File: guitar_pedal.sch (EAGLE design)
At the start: 14 parts, among them P1 RM-065

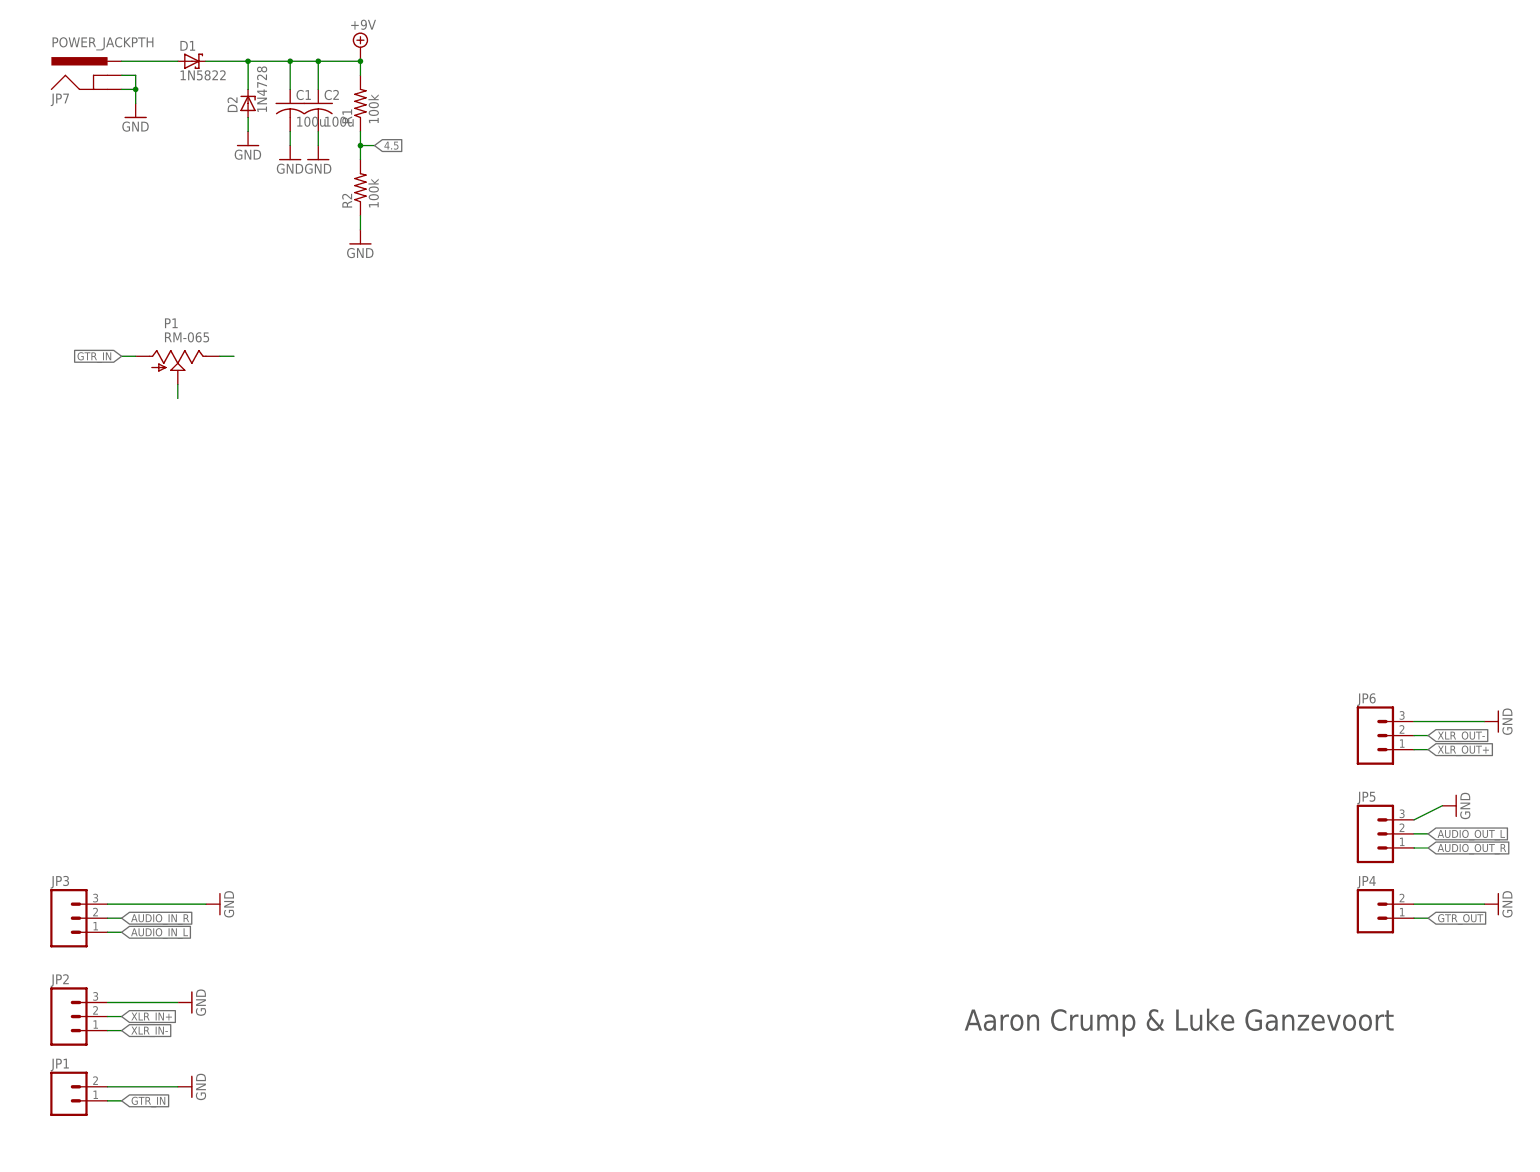
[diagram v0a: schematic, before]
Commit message: mostly finished schematic, still needs stomp switch
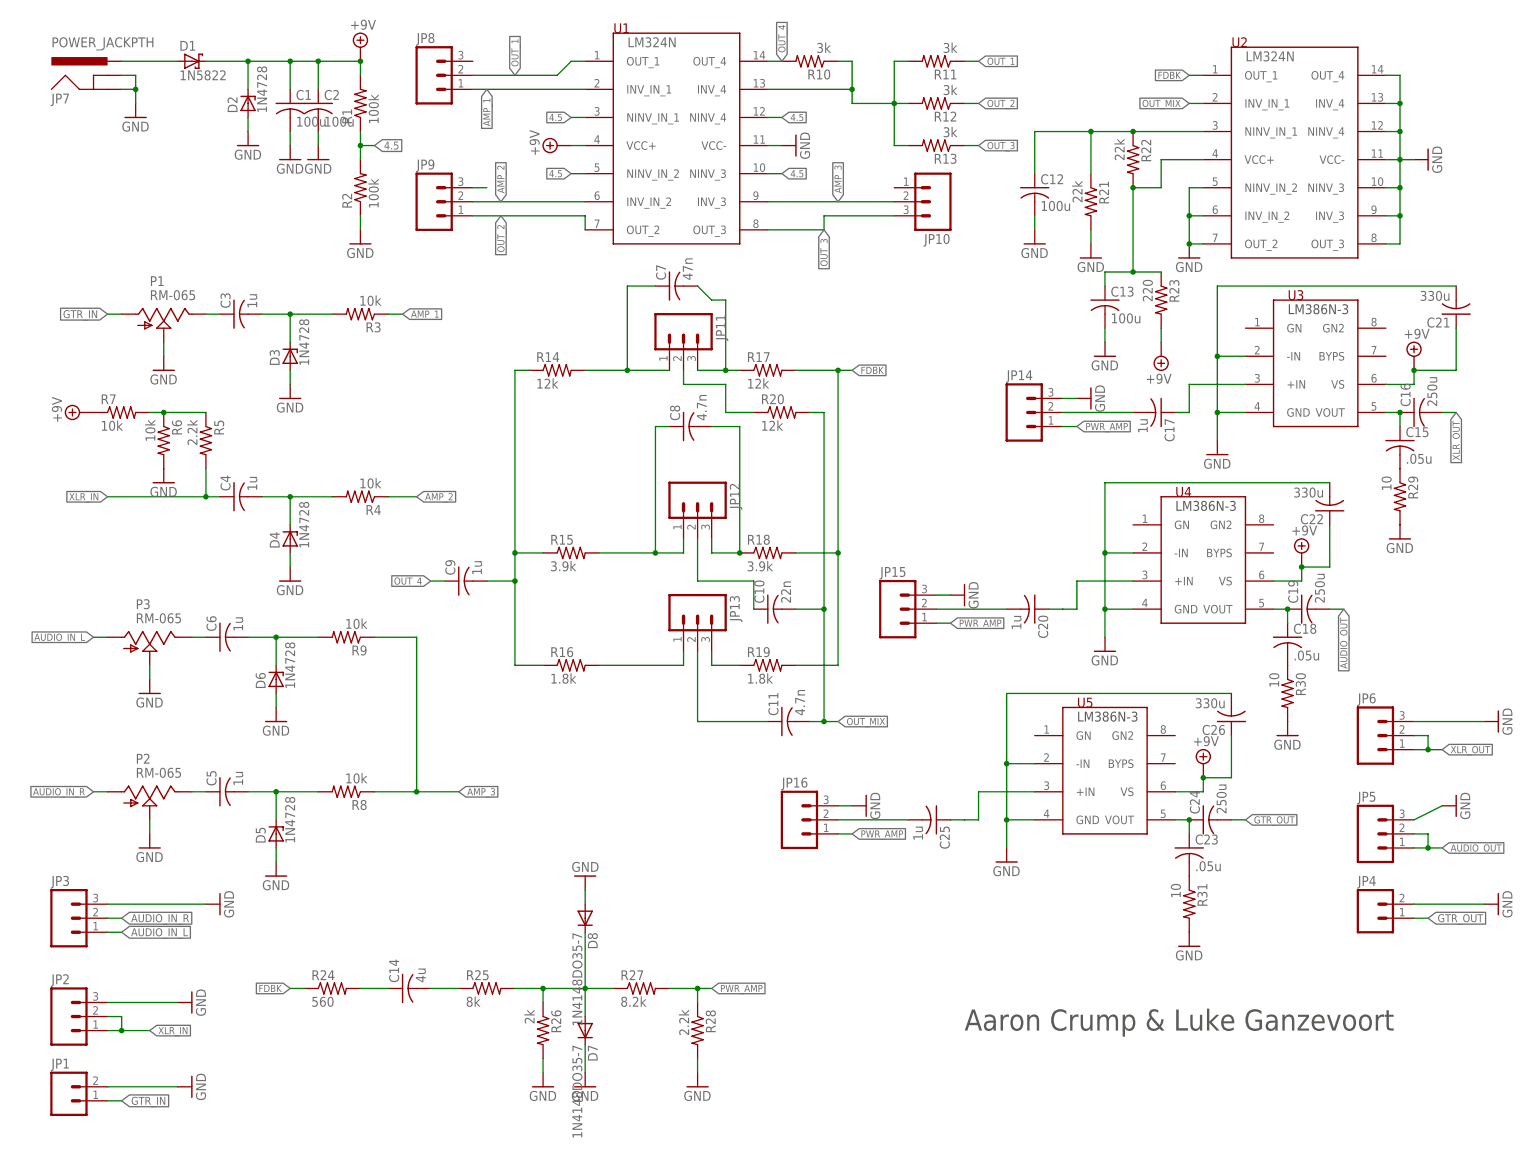
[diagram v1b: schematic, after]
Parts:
- added C10: 22n, resistor:C-USC0805
- added C11, C8: 4.7n, resistor:C-USC0805
- added C12, C13: 100u, resistor:C-USC0805
- added C14: 4u, resistor:C-USC0805
- added C15, C18, C23: .05u, resistor:C-USC0805
- added C16, C19, C24: 250u, resistor:C-USC0805
- added C17, C20, C25, C3, C4, C5, C6, C9: 1u, resistor:C-USC0805
- added C21, C22, C26: 330u, resistor:C-USC0805
- added C7: 47n, resistor:C-USC0805
- added D3, D4, D5, D6: 1N4728, aarons:1N4728
- added D7, D8: 1N4148DO35-7, diode:1N4148DO35-7
- added JP10, JP11, JP12, JP13, JP14, JP15, JP16, JP8, JP9: (no value), SparkFun-Connectors:M03PTH
- added P2, P3: RM-065, aarons:RM-065
- added R10, R11, R12, R13: 3k, resistor:R-US_R0805
- added R14, R17, R20: 12k, resistor:R-US_R0805
- added R15, R18: 3.9k, resistor:R-US_R0805
- added R16, R19: 1.8k, resistor:R-US_R0805
- added R21, R22: 22k, resistor:R-US_R0805
- added R23: 220, resistor:R-US_R0805
- added R24: 560, resistor:R-US_R0805
- added R25: 8k, resistor:R-US_R0805
- added R26: 2k, resistor:R-US_R0805
- added R27: 8.2k, resistor:R-US_R0805
- added R28, R5: 2.2k, resistor:R-US_R0805
- added R29, R30, R31: 10, resistor:R-US_R0805
- added R3, R4, R6, R7, R8, R9: 10k, resistor:R-US_R0805
- added U1, U2: LM324N, aarons:LM324N
- added U3, U4, U5: LM386N-3, aarons:LM386N-3
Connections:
- removed net AUDIO_OUT_L: JP5.2
- removed net AUDIO_OUT_R: JP5.1
- removed net XLR_IN+: JP2.2
- removed net XLR_IN-: JP2.1
- removed net XLR_OUT+: JP6.1
- removed net XLR_OUT-: JP6.2
- new net AMP_1: C3.2, C4.2, C5.2, C6.2, D3.C, D4.C, D5.C, D6.C, JP8.1, R3.1, R3.2, R4.2, R8.2, R9.2, U1.INV_IN_1
- new net AMP_2: JP9.2, JP9.3, R4.1, U1.INV_IN_2
- new net AMP_3: JP10.2, R8.1, R9.1, U1.INV_3
- new net AUDIO_OUT: C19.2, JP5.1, JP5.2
- new net FDBK: R17.2, R18.2, R19.2, R24.1, U2.OUT_1
- new net N$10: C8.1, JP12.1, R15.2
- new net N$11: JP13.1, R16.2
- new net N$12: C9.2, R14.1, R15.1, R16.1
- new net N$13: C11.1, JP13.2
- new net N$14: C14.1, R24.2
- new net N$15: C7.2, JP11.3, R17.1
- new net N$16: C8.2, JP12.3, R18.1
- new net N$17: JP13.3, R19.1
- new net N$18: JP11.2, R20.1
- new net N$19: C10.1, JP12.2
- new net N$20: C14.2, R25.1
- new net N$21: D7.A, D8.C, R25.2, R26.1, R27.1
- new net N$22: C15.2, R29.1
- new net N$23: C17.2, JP14.2
- new net N$24: C13.1, R22.2, R23.1, U2.VCC+
- new net N$25: C18.1, C19.1, U4.VOUT
- new net N$26: C12.1, R21.1, R22.1, U2.NINV_IN_1
- new net N$27: U4.+IN
- new net N$28: C17.1, U3.+IN
- new net N$29: C18.2, R30.1
- new net N$3: R5.1, R6.1, R7.2
- new net N$30: C20.1
- new net N$31: C20.2, JP15.2
- new net N$34: C23.1, C24.1, U5.VOUT
- new net N$35: U5.+IN
- new net N$36: C23.2, R31.1
- new net N$37: C25.1
- new net N$38: C25.2, JP16.2
- new net N$5: C5.1, P2.E
- new net N$6: C6.1, P3.E
- new net N$7: R10.1, R11.2, R12.2, R13.2, U1.INV_4
- new net N$8: C15.1, C16.1, U3.VOUT
- new net N$9: C7.1, JP11.1, R14.2
- new net OUT_1: JP8.2, R11.1, U1.OUT_1
- new net OUT_2: JP9.1, R12.1, U1.OUT_2
- new net OUT_3: JP10.3, R13.1, U1.OUT_3
- new net OUT_4: C9.1, R10.2, U1.OUT_4
- new net OUT_MIX: C10.2, C11.2, R20.2, U2.INV_IN_1
- new net PWR_AMP: JP14.1, JP15.1, JP16.1, R27.2, R28.1
- new net XLR_IN: C4.1, JP2.1, JP2.2, R5.2
- new net XLR_OUT: C16.2, JP6.1, JP6.2
- net +9V: now also C21.1, C22.1, C26.1, R23.2, R7.1, U1.VCC+, U3.VS, U4.VS, U5.VS
- net 4.5: now also U1.NINV_3, U1.NINV_4, U1.NINV_IN_1, U1.NINV_IN_2
- net AUDIO_IN_L: now also P3.A
- net AUDIO_IN_R: now also P2.A
- net GND: now also C12.2, C13.2, C21.2, C22.2, C26.2, D3.A, D4.A, D5.A, D6.A, D7.C, D8.A, JP14.3, JP15.3, JP16.3, R21.2, R26.2, R28.2, R29.2, R30.2, R31.2, R6.2, U1.VCC-, U2.INV_3, U2.INV_4, U2.INV_IN_2, U2.NINV_3, U2.NINV_4, U2.NINV_IN_2, U2.OUT_2, U2.OUT_3, U2.OUT_4, U2.VCC-, U3.-IN, U3.GND, U4.-IN, U4.GND, U5.-IN, U5.GND
- net GTR_OUT: now also C24.2
- net N$2: now also P2.S, P3.S
- net N$4: now also C3.1
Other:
- moved on the sheet: P1

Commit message: Began to organize into different sheets.
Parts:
- C1, C2: value 100u -> 100uF

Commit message: Finished organizing sheets
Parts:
- C1, C2: value 100uF -> 100u
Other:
- moved on the sheet: C15, C16, C17, C18, C19, C20, C21, C22, C23, C24, C25, C26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

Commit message: editted schematic to orgainize and fix mistakes.
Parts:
- removed JP10, JP11, JP12, JP13, JP14, JP15, JP16, JP8, JP9: (no value), SparkFun-Connectors:M03PTH
- added R32: 1A PTC, resistor:R-US_R0805
- added R33, R34, R36, R37, R38, R39, R41: 100k, aarons:POT
- added R35: (no value), aarons:POT
- added R42: 500k, aarons:POT
- C1, C12, C13, C2: value 100u -> 100uF 35v; device resistor:C-USC0805 -> Luke:CAPACITORCAN_6MM
- C10, C11, C17, C20, C25, C3, C4, C5, C6, C7, C8, C9: device resistor:C-USC0805 -> Luke:CAPACITOR0805
- C14: value 4u -> 4uF; device resistor:C-USC0805 -> Luke:CAPACITOR0805
- C21, C22, C26: value 330u -> 470uF; device resistor:C-USC0805 -> Luke:CAP_CAN01
- C24: value 250u -> 250uF 50v
- D2: value 1N4728 -> 1n4739
- R10: value 3k -> 3.3k; device resistor:R-US_R0805 -> Luke:RESISTOR0805
- R11, R12, R13: value 3k -> 10k; device resistor:R-US_R0805 -> Luke:RESISTOR0805
- R14, R15, R16, R17, R18, R19, R20, R21, R22, R23, R24, R25, R26, R27, R28, R3, R4, R5, R6, R7, R8, R9: device resistor:R-US_R0805 -> Luke:RESISTOR0805
- U1: value LM324N -> LM324NSOIC-14; device aarons:LM324N -> aarons:LM324NSOIC-14
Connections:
- removed net N$24: C13.1, R22.2, R23.1, U2.VCC+
- removed net N$30: C20.1
- removed net N$37: C25.1
- new net N$32: D1.C, R32.2
- net +9V: now also C1.POS, C2.POS, C21.POS, C22.POS, C26.POS, R32.1; no longer C1.1, C2.1, C21.1, C22.1, C26.1, D1.C
- net AMP_1: now also C3.NEG, C4.NEG, C5.NEG, C6.NEG, R33.W; no longer C3.2, C4.2, C5.2, C6.2, JP8.1
- net AMP_2: now also R34.W; no longer JP9.2, JP9.3
- net AMP_3: now also R35.W; no longer JP10.2
- net AUDIO_IN_L: now also P3.2; no longer P3.A
- net AUDIO_IN_R: now also P2.2; no longer P2.A
- net GND: now also C1.NEG, C12.NEG, C13.NEG, C2.NEG, C21.NEG, C22.NEG, C26.NEG, P1.1, P2.1, P3.1, R36.1, R37.1, R38.1; no longer C1.2, C12.2, C13.2, C2.2, C21.2, C22.2, C26.2, JP14.3, JP15.3, JP16.3, U2.OUT_2, U2.OUT_3, U2.OUT_4
- net GTR_IN: now also P1.2; no longer P1.A
- net N$10: now also C8.POS, R41.1; no longer C8.1, JP12.1
- net N$11: now also R42.1; no longer JP13.1
- net N$12: now also C9.NEG; no longer C9.2
- net N$13: now also C11.POS, R42.W; no longer C11.1, JP13.2
- net N$14: now also C14.POS; no longer C14.1
- net N$15: now also C7.NEG, R39.2; no longer C7.2, JP11.3
- net N$16: now also C8.NEG, R41.2; no longer C8.2, JP12.3
- net N$17: now also R42.2; no longer JP13.3
- net N$18: now also R39.W; no longer JP11.2
- net N$19: now also C10.POS, R41.W; no longer C10.1, JP12.2
- net N$2: now also C5.POS, P2.W; no longer P1.S, P2.S, P3.S
- net N$20: now also C14.NEG; no longer C14.2
- net N$23: now also C17.NEG, R38.W; no longer C17.2, JP14.2
- net N$26: now also C12.POS; no longer C12.1
- net N$27: now also C20.POS
- net N$28: now also C17.POS; no longer C17.1
- net N$31: now also C20.NEG, R37.W; no longer C20.2, JP15.2
- net N$35: now also C25.POS
- net N$38: now also C25.NEG, R36.W; no longer C25.2, JP16.2
- net N$4: now also C3.POS, P1.W; no longer C3.1, P1.E
- net N$5: now also C13.POS, R22.2, R23.1, U2.VCC+; no longer C5.1, P2.E
- net N$6: now also C6.POS, P3.W; no longer C6.1, P3.E
- net N$9: now also C7.POS, R39.1; no longer C7.1, JP11.1
- net OUT_1: now also R33.1; no longer JP8.2
- net OUT_2: now also R34.1; no longer JP9.1
- net OUT_3: now also R35.2; no longer JP10.3
- net OUT_4: now also C9.POS; no longer C9.1
- net OUT_MIX: now also C10.NEG, C11.NEG; no longer C10.2, C11.2
- net PWR_AMP: now also R36.2, R37.2, R38.2; no longer JP14.1, JP15.1, JP16.1
- net XLR_IN: now also C4.POS; no longer C4.1

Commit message: finished schematic changes
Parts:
- removed R32: 1A PTC, resistor:R-US_R0805
- added C27, C28, C29, C30, C31, C32, C33: 1uF, Luke:CAPACITOR0805
- added F1: PTCBELFUSE_1206, Luke:PTCBELFUSE_1206
- C15, C18, C23: value .05u -> 47nF; device resistor:C-USC0805 -> Luke:CAPACITOR0805
- C16, C19, C24: device resistor:C-USC0805 -> Luke:CAP_CAN01
- D3, D4, D5, D6: value 1N4728 -> 1N4739
- R29, R30, R31: device resistor:R-US_R0805 -> Luke:RESISTOR0805
- R35: value (none) -> 100k
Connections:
- new net N$24: C4.NEG, D4.C, R4.2
- new net N$30: C6.NEG, D6.C, R9.2
- new net N$33: C5.NEG, D5.C, R8.2
- new net N$37: C3.NEG, D3.C, R3.2
- net +9V: now also C27.POS, C28.POS, C31.POS, C32.POS, C33.POS, F1.2; no longer R32.1
- net AMP_1: no longer C3.NEG, C4.NEG, C5.NEG, C6.NEG, D3.C, D4.C, D5.C, D6.C, R3.2, R4.2, R8.2, R9.2
- net AUDIO_OUT: now also C19.NEG; no longer C19.2
- net GND: now also C27.NEG, C28.NEG, C29.NEG, C30.NEG, C31.NEG, C32.NEG, C33.NEG
- net GTR_OUT: now also C24.NEG; no longer C24.2
- net N$22: now also C15.NEG; no longer C15.2
- net N$25: now also C18.POS, C19.POS; no longer C18.1, C19.1
- net N$29: now also C18.NEG; no longer C18.2
- net N$32: now also F1.1; no longer R32.2
- net N$34: now also C23.POS, C24.POS; no longer C23.1, C24.1
- net N$36: now also C23.NEG; no longer C23.2
- net N$5: now also C29.POS, C30.POS
- net N$8: now also C15.POS, C16.POS; no longer C15.1, C16.1
- net XLR_OUT: now also C16.NEG; no longer C16.2
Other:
- moved on the sheet: JP4, JP5, JP6
